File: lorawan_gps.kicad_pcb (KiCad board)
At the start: 2 copper layers, 5 parts, among them U1 MAX-M8, U2 SHT21, U3 MPU-9250, U4 SX1276

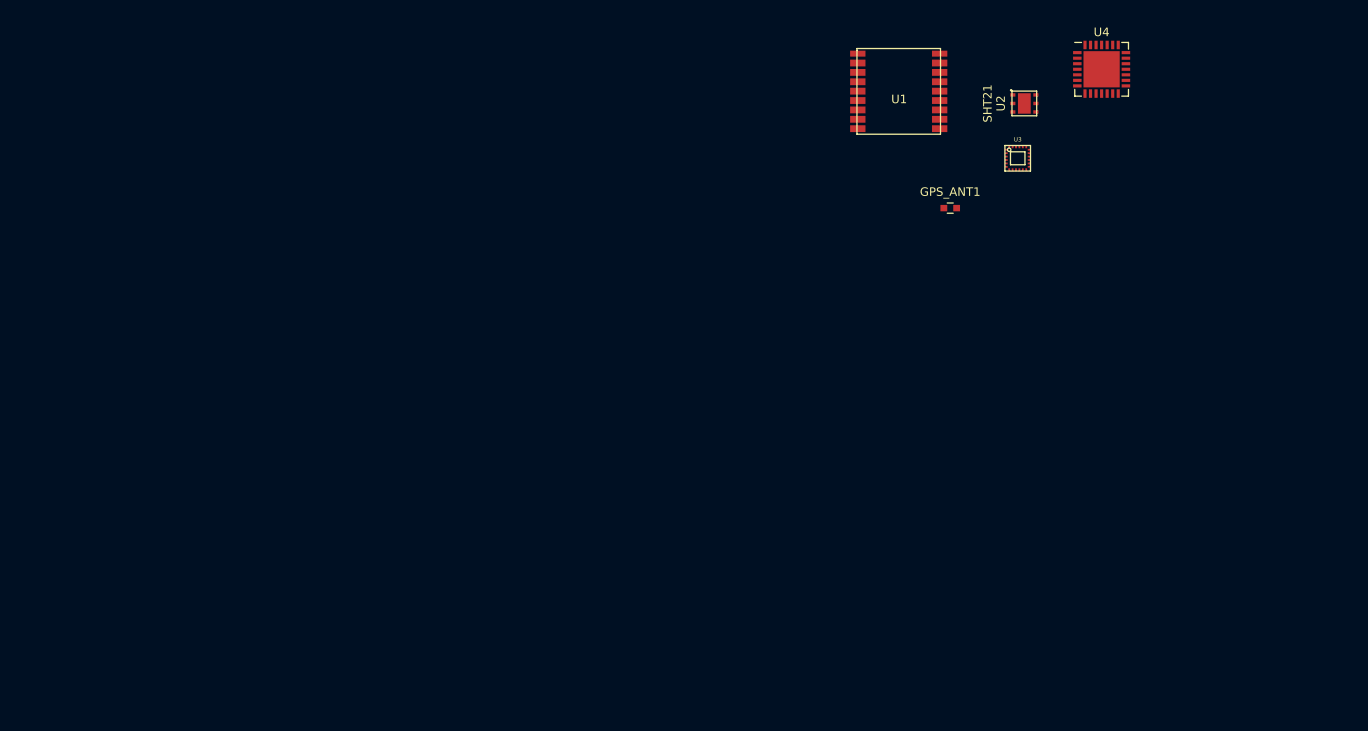
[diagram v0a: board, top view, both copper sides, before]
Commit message: Added outline for AAA battery size
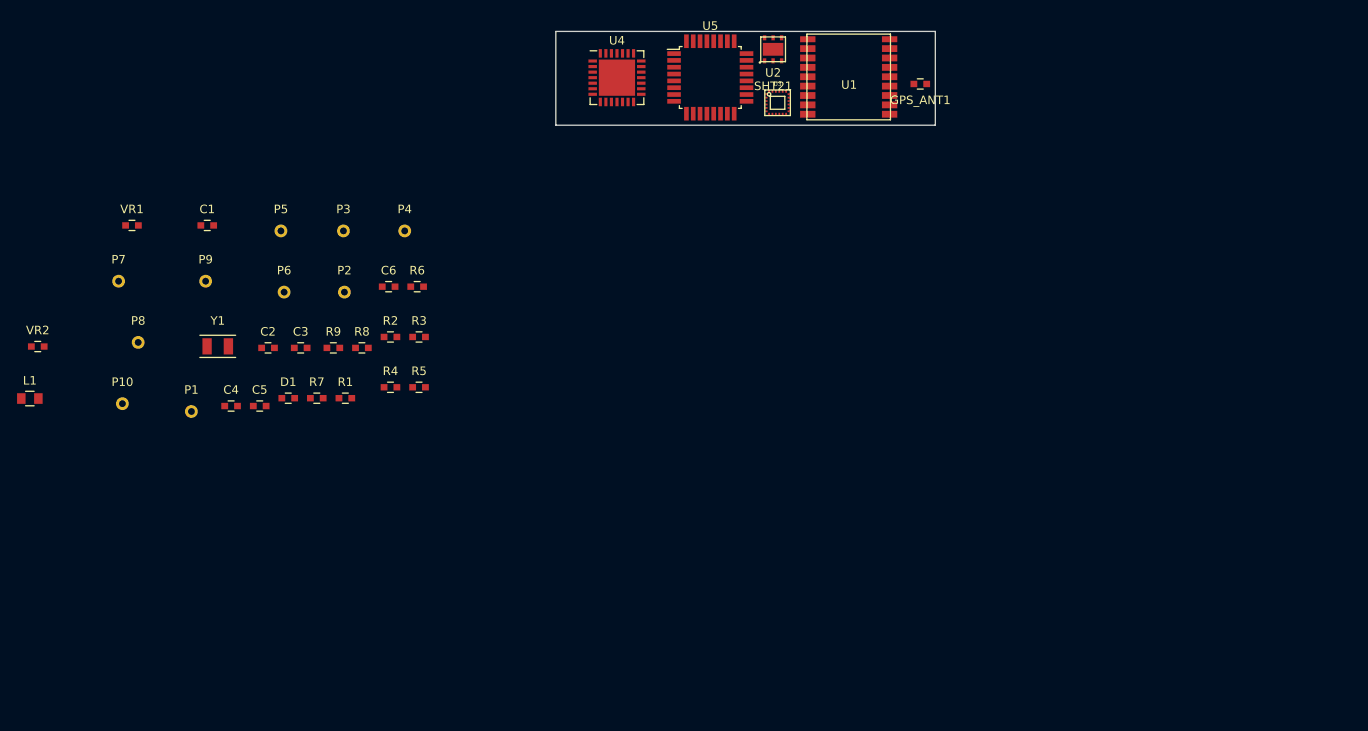
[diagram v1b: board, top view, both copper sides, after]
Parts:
- added C1: 100n, Capacitors_SMD:C_0603, F.Cu at (59.1, 42.8)
- added C2: 1u, Capacitors_SMD:C_0603, F.Cu at (66.2, 57.1)
- added C3: 100n, Capacitors_SMD:C_0603, F.Cu at (70.1, 57.1)
- added C4: 1u, Capacitors_SMD:C_0603, F.Cu at (61.9, 63.9)
- added C5: 22p, Capacitors_SMD:C_0603, F.Cu at (65.3, 63.9)
- added C6: 22p, Capacitors_SMD:C_0603, F.Cu at (80.4, 49.9)
- added D1: LED, Capacitors_SMD:C_0603, F.Cu at (68.6, 63.0)
- added L1: MH2029-300Y, Capacitors_SMD:C_0805, F.Cu at (38.3, 63.1)
- added P1: BL_PAD, Measurement_Points:Measurement_Point_Round-TH_Small, F.Cu at (57.3, 64.6)
- added P10: CONN_01X01, Measurement_Points:Measurement_Point_Round-TH_Small, F.Cu at (49.2, 63.7)
- added P2: SWD_DAT, Measurement_Points:Measurement_Point_Round-TH_Small, F.Cu at (75.2, 50.6)
- added P3: SWD_CLK, Measurement_Points:Measurement_Point_Round-TH_Small, F.Cu at (75.1, 43.4)
- added P4: SWD_3V3, Measurement_Points:Measurement_Point_Round-TH_Small, F.Cu at (82.3, 43.4)
- added P5: SWD_GND, Measurement_Points:Measurement_Point_Round-TH_Small, F.Cu at (67.8, 43.4)
- added P6: SWD_RST, Measurement_Points:Measurement_Point_Round-TH_Small, F.Cu at (68.1, 50.6)
- added P7: CONN_01X01, Measurement_Points:Measurement_Point_Round-TH_Small, F.Cu at (48.7, 49.3)
- added P8: CONN_01X01, Measurement_Points:Measurement_Point_Round-TH_Small, F.Cu at (51.0, 56.5)
- added P9: CONN_01X01, Measurement_Points:Measurement_Point_Round-TH_Small, F.Cu at (58.9, 49.3)
- added R1: 10k, Capacitors_SMD:C_0603, F.Cu at (75.3, 63.0)
- added R2: 2k, Capacitors_SMD:C_0603, F.Cu at (80.6, 55.8)
- added R3: 10k, Capacitors_SMD:C_0603, F.Cu at (84.0, 55.8)
- added R4: 2k, Capacitors_SMD:C_0603, F.Cu at (80.6, 61.7)
- added R5: 10k, Capacitors_SMD:C_0603, F.Cu at (84.0, 61.7)
- added R6: 1k, Capacitors_SMD:C_0603, F.Cu at (83.7, 49.9)
- added R7: 1k, Capacitors_SMD:C_0603, F.Cu at (72.0, 63.0)
- added R8: 1k, Capacitors_SMD:C_0603, F.Cu at (77.3, 57.1)
- added R9: 1k, Capacitors_SMD:C_0603, F.Cu at (73.9, 57.1)
- added U5: SAMD21E17A, Housings_QFP:TQFP-32_7x7mm_Pitch0.8mm, F.Cu at (118.1, 25.4)
- added VR1: CG0603MLC-05E, Capacitors_SMD:C_0603, F.Cu at (50.3, 42.8)
- added VR2: CG0603MLC-05E, Capacitors_SMD:C_0603, F.Cu at (39.2, 57.0)
- added Y1: 32.768kHz, ABS07_abracon:ABS07, F.Cu at (60.3, 56.9)
- moved U4 56.8 mm to (107.2, 25.4)
- moved U2 30.1 mm to (125.5, 22.1), turned to 0 degrees
- moved U3 28.9 mm to (126.0, 28.4)
- moved GPS_ANT1 15.0 mm to (142.7, 26.2), turned to 180 degrees
- moved U1 6.11 mm to (134.3, 20.9)
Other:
- board outline added: 44.5 x 11 mm

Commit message: started layout, completed schematic
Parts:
- added BT1: Battery, Pin_Headers:Pin_Header_Straight_1x02, F.Cu at (142.0, 97.8)
- added C10: 100n, Capacitors_SMD:C_0603, F.Cu at (130.0, 86.9)
- added C11: 1u, Capacitors_SMD:C_0603, F.Cu at (131.8, 83.5)
- added C12: 22p, Capacitors_SMD:C_0603, F.Cu at (129.0, 98.0)
- added C13: 22p, Capacitors_SMD:C_0603, F.Cu at (131.5, 98.0)
- added C14: 10uF, Capacitors_SMD:C_0805, F.Cu at (141.5, 93.9)
- added C15: 100nF, Capacitors_SMD:C_0603, F.Cu at (144.9, 90.1)
- added C16: 100nF, Capacitors_SMD:C_0603, F.Cu at (141.2, 88.0)
- added C17: 10uF, Capacitors_SMD:C_0805, F.Cu at (141.2, 86.2)
- added C18: 10uF, Capacitors_SMD:C_0805, F.Cu at (141.2, 84.0)
- added C19: 100nF, Capacitors_SMD:C_0603, F.Cu at (114.9, 97.5)
- added C20: 33nF, Capacitors_SMD:C_0603, F.Cu at (111.1, 83.1)
- added C7: 100nF, Capacitors_SMD:C_0603, F.Cu at (170.7, 91.0)
- added C8: 100n, Capacitors_SMD:C_0603, F.Cu at (138.1, 93.2)
- added C9: 1u, Capacitors_SMD:C_0603, F.Cu at (130.2, 82.0)
- added IC1: TPS61201, TPS61200:VSON-10-1(4)EP_3x3mm_Pitch0.5mm, F.Cu at (141.8, 91.0)
- added L2: 2.2uH, Capacitors_SMD:C_0805, F.Cu at (138.6, 90.4)
- added L3: INDUCTOR_SMALL, Capacitors_SMD:C_0805, F.Cu at (108.3, 82.5)
- added P11: CONN_01X04, Pin_Headers:Pin_Header_Straight_1x04, F.Cu at (121.7, 93.6)
- added R10: DNF, Capacitors_SMD:C_0603, F.Cu at (144.6, 87.8)
- added R11: DNF, Capacitors_SMD:C_0603, F.Cu at (144.6, 86.2)
- added SW1: SW_PUSH, Buttons_Switches_SMD:SW_SPST_EVQP2, F.Cu at (136.2, 97.8)
- added SW2: SW_PUSH, Buttons_Switches_SMD:SW_SPST_EVQP2, F.Cu at (124.5, 97.8)
- C1: value 100n -> 100nF
- C2, C4: value 1u -> 100nF
- C3: value 100n -> 10nF
- C5: value 22p -> LoRa Ant; footprint Capacitors_SMD:C_0603 -> Capacitors_SMD:C_1206
- C6: value 22p -> 10uF; footprint Capacitors_SMD:C_0603 -> Capacitors_SMD:C_0805
- GPS_ANT1: footprint Capacitors_SMD:C_0603 -> Capacitors_SMD:C_1206
- L1: value MH2029-300Y -> 100R; footprint Capacitors_SMD:C_0805 -> Capacitors_SMD:C_0603
- R2: value 2k -> 10k
- R3: value 10k -> 2k
- R4: value 2k -> 1k
- R5: value 10k -> 1k
- R7: value 1k -> 2M
- R8: value 1k -> 220K
- R9: value 1k -> 10R
- U1: value MAX-M8 -> SHT21; footprint _sensors:MAX-M8 -> timhawes:SHT21
- U2: value SHT21 -> MPU-9250; footprint timhawes:SHT21 -> mpu-9250:MPU-9250
- U3: value MPU-9250 -> RFM9xW; footprint mpu-9250:MPU-9250 -> RFM95W:RFM9xW
- U4: value SX1276 -> SAMD21E17A; footprint Housings_DFN_QFN:QFN-28-1EP_6x6mm_Pitch0.65mm -> Housings_DFN_QFN:QFN-32-1EP_5x5mm_Pitch0.5mm
- U5: value SAMD21E17A -> MAX-M8; footprint Housings_QFP:TQFP-32_7x7mm_Pitch0.8mm -> _sensors:MAX-M8
- moved C5 113.1 mm to (173.5, 96.6), turned to 270 degrees
- moved L1 104.8 mm to (138.1, 94.8)
- moved VR2 99.5 mm to (135.0, 83.8), turned to 90 degrees
- moved VR1 95.6 mm to (136.6, 83.8), turned to 90 degrees
- moved P8 92.4 mm to (138.4, 86.4)
- moved P9 86.7 mm to (138.4, 83.8)
- moved C1 81.3 mm to (125.2, 90.2)
- moved Y1 79.7 mm to (130.2, 95.2), turned to 180 degrees
- moved P7 79.2 mm to (123.2, 76.2)
- moved R7 79.0 mm to (145.0, 93.2), turned to 90 degrees
- moved P10 76.9 mm to (118.1, 97.8)
- moved GPS_ANT1 73.2 mm to (102.4, 87.3), turned to 0 degrees
- moved P4 73.1 mm to (144.8, 81.3)
- moved U1 73.0 mm to (125.2, 93.3)
- moved R8 72.7 mm to (144.6, 84.5)
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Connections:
- net /MCU/5V_USB renamed Net-(P7-Pad1)
- C5 pad 2: GND -> Net-(C5-Pad2)
- C6 pad 1: GND -> +3V3
- C6 pad 2: Net-(C6-Pad2) -> GND
- R1 pad 1: /MCU/5VSenseIn -> +3V3
- R1 pad 2: /MCU/5VDiv -> /MCU/#RESET
- R2 pad 1: /MCU/5VDiv -> /Battery/V_BAT
- R2 pad 2: GND -> /MCU/AIN_6
- R3 pad 1: /MCU/VbatIN -> /MCU/AIN_6
- R3 pad 2: /MCU/VbatDiv -> GND
- R4 pad 1: /MCU/VbatDiv -> +3V3
- R4 pad 2: GND -> Net-(D1-Pad2)
- R5 pad 2: /MCU/#RESET -> /MCU/MPU_SDA
- R6 pad 2: /MCU/intb -> /MCU/MPU_SCL
- R7 pad 1: +3V3 -> /Battery/V_BAT
- R7 pad 2: /MCU/SDA -> Net-(C15-Pad2)
- R8 pad 1: +3V3 -> Net-(C15-Pad2)
- R8 pad 2: /MCU/SCL -> GND
- R9 pad 1: +3V3 -> Net-(C20-Pad1)
- R9 pad 2: Net-(D1-Pad2) -> Net-(R9-Pad2)
- U1 pad 1: Net-(U1-Pad1) -> /MCU/MPU_SDA
- U1 pad 2: Net-(U1-Pad2) -> GND
- U1 pad 5: Net-(U1-Pad5) -> +3V3
- U1 pad 6: Net-(U1-Pad6) -> /MCU/MPU_SCL
- U2 pad 1: Net-(U2-Pad1) -> +3V3
- U3 pad 1: Net-(U3-Pad1) -> GND
- U3 pad 10: Net-(U3-Pad10) -> GND
- U3 pad 13: Net-(U3-Pad13) -> +3V3
- U3 pad 14: Net-(U3-Pad14) -> /MCU/MPU_INT9
- U3 pad 15: Net-(U3-Pad15) -> /MCU/MPU_IN14
- U3 pad 16: Net-(U3-Pad16) -> /MCU/MPU_INT5
- U3 pad 2: Net-(U3-Pad2) -> /MCU/MPU_MISO
- U3 pad 3: Net-(U3-Pad3) -> /MCU/MPU_MOSI
- U3 pad 4: Net-(U3-Pad4) -> /MCU/MPU_SCK
- U3 pad 5: Net-(U3-Pad5) -> /MCU/MPU_SS
- U3 pad 6: Net-(U3-Pad6) -> /MCU/MPU_D14
- U3 pad 8: Net-(U3-Pad8) -> GND
- U3 pad 9: Net-(U3-Pad9) -> Net-(C5-Pad2)
- U4 pad 1: Net-(U4-Pad1) -> Net-(C12-Pad1)
- U4 pad 10: Net-(U4-Pad10) -> GND
- U4 pad 12: Net-(U4-Pad12) -> /MCU/MPU_INT9
- U4 pad 13: Net-(U4-Pad13) -> /MCU/MPU_TX1
- U4 pad 14: Net-(U4-Pad14) -> /MCU/MPU_RX1
- U4 pad 15: Net-(U4-Pad15) -> /MCU/MPU_D14
- U4 pad 16: Net-(U4-Pad16) -> /MCU/MPU_IN14
- U4 pad 17: Net-(U4-Pad17) -> /MCU/MPU_SDA
- U4 pad 18: Net-(U4-Pad18) -> /MCU/MPU_SCL
- U4 pad 19: Net-(U4-Pad19) -> /MCU/MPU_MOSI
- U4 pad 2: Net-(U4-Pad2) -> Net-(C13-Pad2)
- U4 pad 20: Net-(U4-Pad20) -> /MCU/MPU_SCK
- U4 pad 21: Net-(U4-Pad21) -> /MCU/MPU_MISO
- U4 pad 22: Net-(U4-Pad22) -> /MCU/MPU_SS
- U4 pad 23: Net-(U4-Pad23) -> Net-(P8-Pad1)
- U4 pad 24: Net-(U4-Pad24) -> Net-(P9-Pad1)
- U4 pad 25: Net-(U4-Pad25) -> Net-(P1-Pad1)
- U4 pad 26: Net-(U4-Pad26) -> /MCU/#RESET
- U4 pad 27: Net-(U4-Pad27) -> Net-(D1-Pad1)
- U4 pad 28: Net-(U4-Pad28) -> GND
- U4 pad 29: (no net) -> Net-(C11-Pad1)
- U4 pad 5: Net-(U4-Pad5) -> /9axis/INT_9AXIS
- U4 pad 6: Net-(U4-Pad6) -> /MCU/MPU_INT5
- U4 pad 7: Net-(U4-Pad7) -> /MCU/AIN_6
- U4 pad 9: Net-(U4-Pad9) -> Net-(L1-Pad1)
- U5 pad 1: Net-(C5-Pad1) -> GND
- U5 pad 11: Net-(U5-Pad11) -> /GPS/GPS_FEEDER
- U5 pad 12: Net-(U5-Pad12) -> GND
- U5 pad 14: Net-(U5-Pad14) -> Net-(R9-Pad2)
- U5 pad 15: /MCU/intb -> Net-(U5-Pad15)
- U5 pad 16: /MCU/PZTEnable -> /MCU/MPU_SDA
- U5 pad 17: /MCU/SDA -> /MCU/MPU_SCL
- U5 pad 18: /MCU/SCL -> Net-(U5-Pad18)
- U5 pad 2: Net-(C6-Pad2) -> /MCU/MPU_RX1
- U5 pad 3: Net-(U5-Pad3) -> /MCU/MPU_TX1
- U5 pad 4: Net-(D1-Pad1) -> Net-(U5-Pad4)
- U5 pad 6: /MCU/VbatDiv -> +3V3
- U5 pad 7: /MCU/5VDiv -> +3V3
- U5 pad 8: Net-(U5-Pad8) -> +3V3
- U5 pad 9: Net-(L1-Pad1) -> +3V3
- Y1 pad 1: Net-(C5-Pad1) -> Net-(C13-Pad2)
- Y1 pad 2: Net-(C6-Pad2) -> Net-(C12-Pad1)
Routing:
- net +3V3: track 0.00 -> 110.8 mm, vias 0 -> 8
- net GND: track 0.00 -> 67.8 mm, vias 0 -> 11
- net /MCU/MPU_INT5: track 0.00 -> 48.3 mm, vias 0 -> 2
- net /MCU/MPU_INT9: track 0.00 -> 39.7 mm, vias 0 -> 2
- net /MCU/MPU_IN14: track 0.00 -> 37.1 mm, vias 0 -> 2
- net /MCU/MPU_SDA: track 0.00 -> 34.8 mm, vias 0 -> 4
- net /MCU/MPU_TX1: track 0.00 -> 31.5 mm, vias 0 -> 2
- net /MCU/MPU_SS: track 0.00 -> 30.8 mm, vias 0 -> 2
- net /MCU/MPU_RX1: track 0.00 -> 28.1 mm, vias 0 -> 2
- net /MCU/MPU_SCK: track 0.00 -> 24.1 mm, vias 0 -> 2
- net /Battery/V_BAT: track 0.00 -> 23.5 mm, vias 0 -> 1
- net /MCU/MPU_SCL: track 0.00 -> 23.3 mm, vias 0 -> 2
- net /9axis/INT_9AXIS: track 0.00 -> 22.7 mm, vias 0 -> 2
- net /MCU/MPU_MISO: track 0.00 -> 19.9 mm, vias 0 -> 2
- net /MCU/MPU_D14: track 0.00 -> 18.1 mm, vias 0 -> 2
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- added copper zone on F.Cu, net +3V3
- added copper zone on F.Cu, net /Battery/V_BAT
- added copper zone on B.Cu, net GND
- added copper zone on F.Cu, net GND
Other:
- board size 44.5 x 11 mm -> 75 x 20 mm
- net class Default: via_drill 0.4 -> 0.3
- rule trace_min: 0.2 -> 0.25
- rule via_min_size: 0.4 -> 0.6

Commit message: All connected
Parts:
- moved C1 3.76 mm to (127.3, 93.3), turned to 270 degrees
- moved R5 2.94 mm to (125.3, 90.1), turned to 180 degrees
- moved C3 1.33 mm to (122.1, 82.0), turned to 270 degrees
- moved C2 0.84 mm to (123.4, 82.0), turned to 270 degrees
- moved C4 0.78 mm to (116.1, 82.1)
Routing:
- net GND: track 67.8 -> 156.7 mm, vias 11 -> 17
- net +3V3: track 110.8 -> 170.3 mm, vias 8 -> 12
- net /MCU/MPU_SCL: track 23.3 -> 58.9 mm
- net /MCU/MPU_SDA: track 34.8 -> 64.8 mm, vias 4 -> 5
- net Net-(R9-Pad2): track 0.00 -> 11.3 mm
- net Net-(C5-Pad2): track 0.00 -> 10.4 mm
- net /GPS/GPS_FEEDER: track 0.00 -> 9.48 mm
- net /Battery/V_BAT: track 23.5 -> 32.5 mm, vias 1 -> 3
- net Net-(SW2-Pad1): track 12.2 -> 19.9 mm
- net Net-(SW1-Pad1): track 5.10 -> 11.0 mm
- net Net-(C12-Pad1): track 12.6 -> 8.56 mm
- net Net-(C20-Pad1): track 0.00 -> 3.51 mm
- net /MCU/MPU_MISO: track 19.9 -> 22.7 mm
- net Net-(C4-Pad1): track 0.00 -> 2.22 mm
- net /MCU/MPU_SS: track 30.8 -> 31.5 mm
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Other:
- rule trace_min: 0.25 -> 0.16

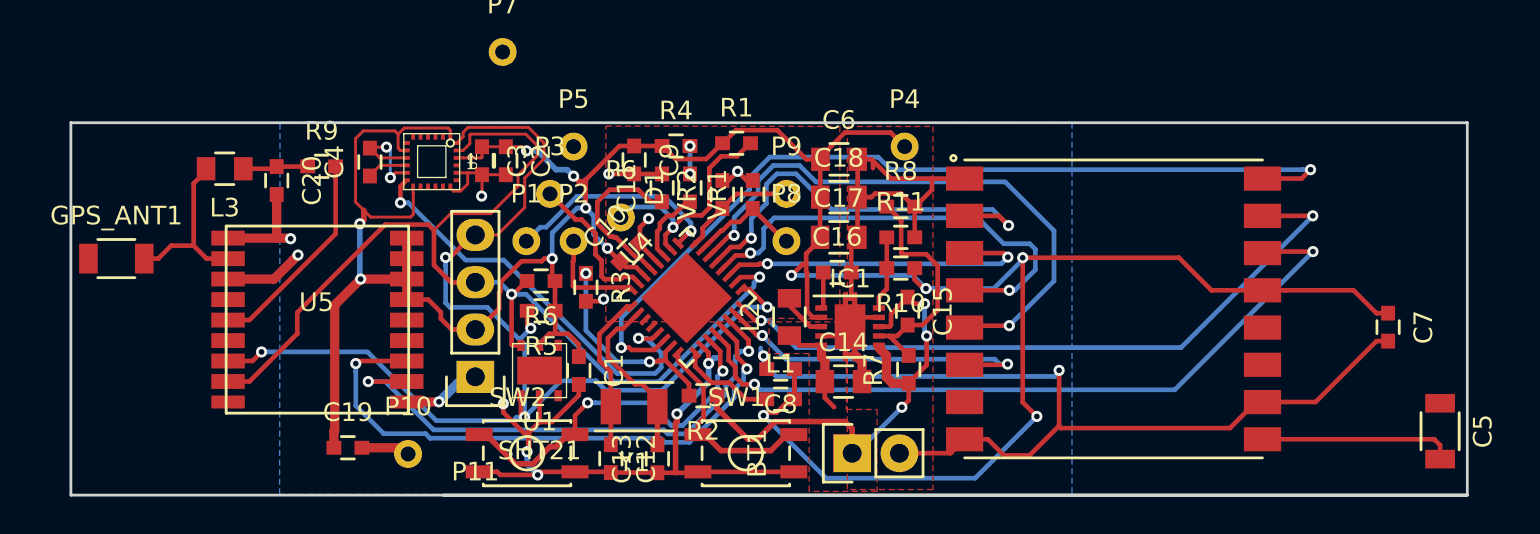
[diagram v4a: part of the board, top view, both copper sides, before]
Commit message: Added Edge-mount SMA connectors to layout - NOTE: 1 UNCONNECT
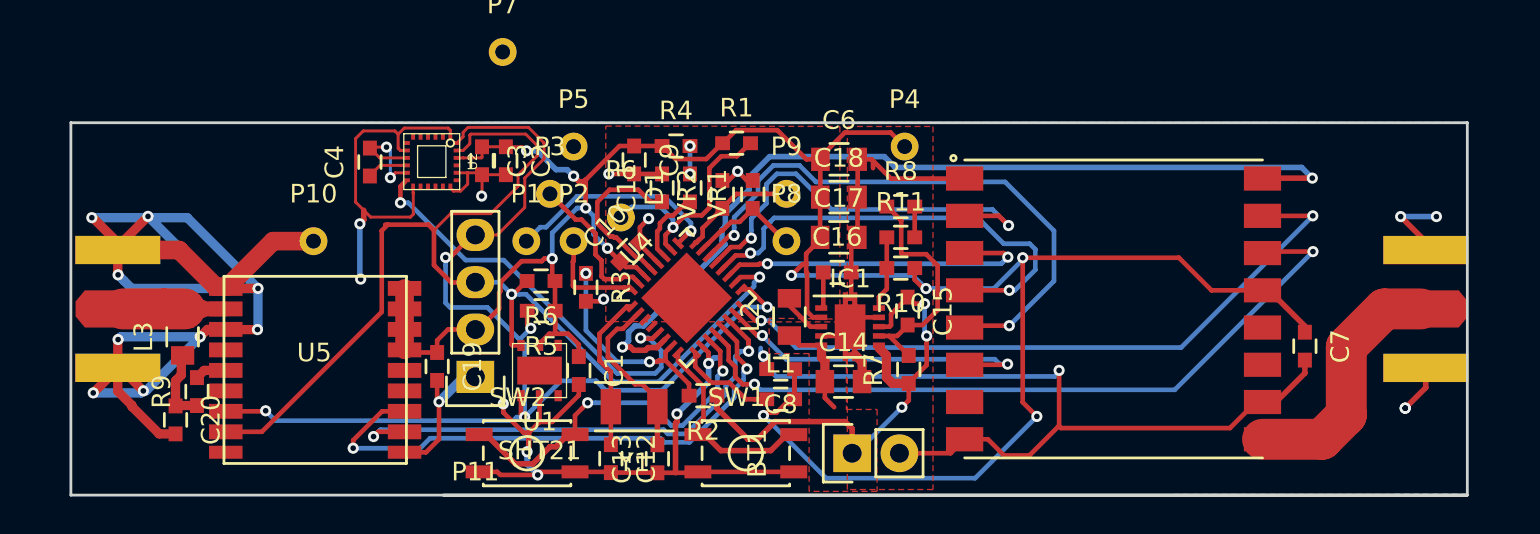
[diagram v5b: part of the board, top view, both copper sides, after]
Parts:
- removed C5: LoRa Ant, Capacitors_SMD:C_1206
- removed GPS_ANT1: C, Capacitors_SMD:C_1206
- added SMA_E1: SMA_EDGE, SMA_EDGE:SMA_EDGE, B.Cu at (93.6, 88.7)
- added SMA_E2: SMA_EDGE, SMA_EDGE:SMA_EDGE, B.Cu at (181.6, 91.3)
- moved C20 14.0 mm to (105.6, 96.0)
- moved R9 13.8 mm to (106.8, 94.4), turned to 90 degrees
- moved P10 12.5 mm to (113.0, 86.4)
- moved L3 9.31 mm to (106.0, 91.5), turned to 90 degrees
- moved C19 6.48 mm to (119.7, 93.1), turned to 270 degrees
- moved C7 4.58 mm to (166.3, 92.0)
- moved U5 2.70 mm to (113.1, 97.7)
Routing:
- net GND: track 156.7 -> 218.4 mm, vias 17 -> 28
- net +3V3: track 170.3 -> 154.5 mm
- net Net-(R9-Pad2): track 11.3 -> 1.71 mm
- net Net-(SMA_E2-Pad1): track 10.4 -> 15.8 mm
- net /MCU/MPU_SCL: track 58.9 -> 62.2 mm
- net /MCU/MPU_TX1: track 31.9 -> 30.3 mm
- net /MCU/MPU_RX1: track 28.5 -> 27.0 mm
- net /MCU/MPU_SDA: track 64.8 -> 63.6 mm
- net /GPS/GPS_FEEDER: track 9.48 -> 8.70 mm
- net /MCU/MPU_INT5: track 48.3 -> 48.8 mm
- net Net-(C20-Pad1): track 3.51 -> 4.03 mm
